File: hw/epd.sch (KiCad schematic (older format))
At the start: 26 parts, among them J1 Conn_01x24_MountingPin, Q2 Q_PMOS_GSD, Q3 IRLML6344, U2 LM75C

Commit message: epd-clock: hw v0.2
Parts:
- removed R4: 0, Resistor_SMD:R_0603_1608Metric, symbol Device:R
- added JP3: Jumper_3_Open, Jumper:SolderJumper-3_P1.3mm_Bridged12_RoundedPad1.0x1.5mm, symbol Jumper:Jumper_3_Open
- Q3: footprint Package_TO_SOT_SMD:SOT-23 -> Package_TO_SOT_SMD:SOT-323_SC-70
- renumbered R5 to R2, R6 to R3, R7 to R4
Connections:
- net BS1: now also JP3.2 (C)
- net GND: now also JP3.1 (A)
- net VCC: now also JP3.3 (B)
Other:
- note added: "3 wire spi"
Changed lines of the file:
@@
 $EndComp
 $Comp
-L power:GND #PWR024
+L power:GND #PWR025
 U 1 1 60F2B86E
 P 6900 2800
-F 0 "#PWR024" H 6900 2550 50  0001 C CNN
+F 0 "#PWR025" H 6900 2550 50  0001 C CNN
 F 1 "GND" H 6905 2627 50  0000 C CNN
 F 2 "" H 6900 2800 50  0001 C CNN
@@
 VGL
 $Comp
-L Device:R R5
+L Device:R R2
 U 1 1 60F42FB6
 P 5800 3300
-F 0 "R5" V 5700 3300 50  0000 C CNN
+F 0 "R2" V 5700 3300 50  0000 C CNN
 F 1 "4.7K" V 5900 3300 50  0000 C CNN
 F 2 "Resistor_SMD:R_0603_1608Metric" V 5730 3300 50  0001 C CNN
@@
 $EndComp
 $Comp
-L Device:R R6
+L Device:R R3
 U 1 1 60F4F067
 P 5800 3650
-F 0 "R6" V 5700 3650 50  0000 C CNN
+F 0 "R3" V 5700 3650 50  0000 C CNN
 F 1 "4.7K" V 5900 3650 50  0000 C CNN
 F 2 "Resistor_SMD:R_0603_1608Metric" V 5730 3650 50  0001 C CNN
@@
 F 0 "Q3" V 6342 5200 50  0000 C CNN
 F 1 "IRLML6344" V 6251 5200 50  0000 C CNN
-F 2 "Package_TO_SOT_SMD:SOT-23" H 6200 5300 50  0001 C CNN
+F 2 "Package_TO_SOT_SMD:SOT-323_SC-70" H 6200 5300 50  0001 C CNN
 F 3 "~" H 6000 5200 50  0001 C CNN
 	1    6000 5200
@@
 	6000 5400 6200 5400
 $Comp
-L Device:R R7
+L Device:R R4
 U 1 1 60FABFF4
 P 6300 4700
-F 0 "R7" H 6370 4746 50  0000 L CNN
+F 0 "R4" H 6370 4746 50  0000 L CNN
 F 1 "4.7" H 6370 4655 50  0000 L CNN
 F 2 "Resistor_SMD:R_0603_1608Metric" V 6230 4700 50  0001 C CNN
@@
 RESE
 $Comp
-L power:GND #PWR022
+L power:GND #PWR023
 U 1 1 60FAFD2B
 P 6300 4450
-F 0 "#PWR022" H 6300 4200 50  0001 C CNN
+F 0 "#PWR023" H 6300 4200 50  0001 C CNN
 F 1 "GND" H 6305 4277 50  0000 C CNN
 F 2 "" H 6300 4450 50  0001 C CNN
@@
 $EndComp
 $Comp
-L power:GND #PWR028
+L power:GND #PWR029
 U 1 1 60F34CE9
 P 8450 4200
-F 0 "#PWR028" H 8450 3950 50  0001 C CNN
+F 0 "#PWR029" H 8450 3950 50  0001 C CNN
 F 1 "GND" H 8455 4027 50  0000 C CNN
 F 2 "" H 8450 4200 50  0001 C CNN
@@
 $EndComp
 NoConn ~ 3300 2600
-Text Label 4200 3400 2    50   ~ 0
+Text Label 4500 3550 2    50   ~ 0
 BS1
-Text Notes 4300 3300 0    50   ~ 0
+Text Notes 4850 3350 0    50   ~ 0
 4 wire spi
 Text Label 4900 4400 0    50   ~ 0
@@
 $EndComp
 $Comp
-L power:GND #PWR013
+L power:GND #PWR014
 U 1 1 6105A8A0
 P 5000 2800
-F 0 "#PWR013" H 5000 2550 50  0001 C CNN
+F 0 "#PWR014" H 5000 2550 50  0001 C CNN
 F 1 "GND" H 5005 2627 50  0000 C CNN
 F 2 "" H 5000 2800 50  0001 C CNN
@@
 VPP
 $Comp
-L power:GND #PWR021
+L power:GND #PWR022
 U 1 1 6102F49A
 P 6200 2800
-F 0 "#PWR021" H 6200 2550 50  0001 C CNN
+F 0 "#PWR022" H 6200 2550 50  0001 C CNN
 F 1 "GND" H 6205 2627 50  0000 C CNN
 F 2 "" H 6200 2800 50  0001 C CNN
@@
 $EndComp
 $Comp
-L power:GND #PWR018
+L power:GND #PWR019
 U 1 1 60F2BEE7
 P 5825 2800
-F 0 "#PWR018" H 5825 2550 50  0001 C CNN
+F 0 "#PWR019" H 5825 2550 50  0001 C CNN
 F 1 "GND" H 5830 2627 50  0000 C CNN
 F 2 "" H 5825 2800 50  0001 C CNN
@@
 $EndComp
 $Comp
-L power:VCC #PWR029
+L power:VCC #PWR030
 U 1 1 610F51AE
 P 8650 3600
-F 0 "#PWR029" H 8650 3450 50  0001 C CNN
+F 0 "#PWR030" H 8650 3450 50  0001 C CNN
 F 1 "VCC" H 8550 3750 50  0000 L CNN
 F 2 "" H 8650 3600 50  0001 C CNN
@@
 $EndComp
 $Comp
-L power:VCC #PWR016
+L power:VCC #PWR017
 U 1 1 61124FF6
 P 5400 5850
-F 0 "#PWR016" H 5400 5700 50  0001 C CNN
+F 0 "#PWR017" H 5400 5700 50  0001 C CNN
 F 1 "VCC" V 5400 5975 50  0000 L CNN
 F 2 "" H 5400 5850 50  0001 C CNN
@@
 $EndComp
 $Comp
-L power:GND #PWR023
+L power:GND #PWR024
 U 1 1 611B06C7
 P 6550 2800
-F 0 "#PWR023" H 6550 2550 50  0001 C CNN
+F 0 "#PWR024" H 6550 2550 50  0001 C CNN
 F 1 "GND" H 6555 2627 50  0000 C CNN
 F 2 "" H 6550 2800 50  0001 C CNN
@@
 $EndComp
 $Comp
-L power:GND #PWR025
+L power:GND #PWR026
 U 1 1 611B425C
 P 7250 2800
-F 0 "#PWR025" H 7250 2550 50  0001 C CNN
+F 0 "#PWR026" H 7250 2550 50  0001 C CNN
 F 1 "GND" H 7255 2627 50  0000 C CNN
 F 2 "" H 7250 2800 50  0001 C CNN
@@
 $EndComp
 $Comp
-L power:VCC #PWR026
+L power:VCC #PWR027
 U 1 1 611B867C
 P 7950 3200
-F 0 "#PWR026" H 7950 3050 50  0001 C CNN
+F 0 "#PWR027" H 7950 3050 50  0001 C CNN
 F 1 "VCC" H 7965 3373 50  0000 C CNN
 F 2 "" H 7950 3200 50  0001 C CNN
@@
 $EndComp
 $Comp
-L power:VCC #PWR019
+L power:VCC #PWR020
 U 1 1 611BC164
 P 5950 3300
-F 0 "#PWR019" H 5950 3150 50  0001 C CNN
+F 0 "#PWR020" H 5950 3150 50  0001 C CNN
 F 1 "VCC" V 5965 3428 50  0000 L CNN
 F 2 "" H 5950 3300 50  0001 C CNN
@@
 $EndComp
 $Comp
-L power:VCC #PWR020
+L power:VCC #PWR021
 U 1 1 611C3951
 P 5950 3650
-F 0 "#PWR020" H 5950 3500 50  0001 C CNN
+F 0 "#PWR021" H 5950 3500 50  0001 C CNN
 F 1 "VCC" V 5965 3778 50  0000 L CNN
 F 2 "" H 5950 3650 50  0001 C CNN
@@
 $EndComp
 $Comp
-L Device:R R4
-U 1 1 60FEDBD7
-P 4500 3400
-F 0 "R4" V 4550 3550 50  0000 C CNN
-F 1 "0" V 4500 3400 50  0000 C CNN
-F 2 "Resistor_SMD:R_0603_1608Metric" V 4430 3400 50  0001 C CNN
-F 3 "~" H 4500 3400 50  0001 C CNN
-	1    4500 3400
-	0    1    1    0
-$EndComp
-$Comp
 L power:GND #PWR012
 U 1 1 611E4B10
-P 4700 3400
-F 0 "#PWR012" H 4700 3150 50  0001 C CNN
-F 1 "GND" V 4705 3272 50  0000 R CNN
-F 2 "" H 4700 3400 50  0001 C CNN
-F 3 "" H 4700 3400 50  0001 C CNN
-	1    4700 3400
-	0    -1   -1   0
+P 4650 3300
+F 0 "#PWR012" H 4650 3050 50  0001 C CNN
+F 1 "GND" H 4550 3200 50  0000 R CNN
+F 2 "" H 4650 3300 50  0001 C CNN
+F 3 "" H 4650 3300 50  0001 C CNN
+	1    4650 3300
+	-1   0    0    1
 $EndComp
 Wire Wire Line
@@
 	8350 3800 8350 4200
 $Comp
-L power:GND #PWR015
+L power:GND #PWR016
 U 1 1 611EE51A
 P 5000 5650
-F 0 "#PWR015" H 5000 5400 50  0001 C CNN
+F 0 "#PWR016" H 5000 5400 50  0001 C CNN
 F 1 "GND" V 5005 5522 50  0000 R CNN
 F 2 "" H 5000 5650 50  0001 C CNN
@@
 $EndComp
 $Comp
-L power:GND #PWR017
+L power:GND #PWR018
 U 1 1 611FBD36
 P 5450 2800
-F 0 "#PWR017" H 5450 2550 50  0001 C CNN
+F 0 "#PWR018" H 5450 2550 50  0001 C CNN
 F 1 "GND" H 5455 2627 50  0000 C CNN
 F 2 "" H 5450 2800 50  0001 C CNN
@@
 	5400 4100 5400 4600
 $Comp
-L power:GND #PWR014
+L power:GND #PWR015
 U 1 1 6121586C
 P 5000 4100
-F 0 "#PWR014" H 5000 3850 50  0001 C CNN
+F 0 "#PWR015" H 5000 3850 50  0001 C CNN
 F 1 "GND" V 5005 3972 50  0000 R CNN
 F 2 "" H 5000 4100 50  0001 C CNN
@@
 $EndComp
 $Comp
-L power:GND #PWR027
+L power:GND #PWR028
 U 1 1 61226EC7
 P 7950 4200
-F 0 "#PWR027" H 7950 3950 50  0001 C CNN
+F 0 "#PWR028" H 7950 3950 50  0001 C CNN
 F 1 "GND" H 7955 4027 50  0000 C CNN
 F 2 "" H 7950 4200 50  0001 C CNN
@@
 $EndComp
 $Comp
-L power:GND #PWR030
+L power:GND #PWR031
 U 1 1 6122A035
 P 8650 3900
-F 0 "#PWR030" H 8650 3650 50  0001 C CNN
+F 0 "#PWR031" H 8650 3650 50  0001 C CNN
 F 1 "GND" H 8655 3727 50  0000 C CNN
 F 2 "" H 8650 3900 50  0001 C CNN
@@
 	1    0    0    -1
 $EndComp
-Wire Wire Line
-	4650 3400 4700 3400
-$Comp
-L power:PWR_FLAG #FLG03
+$Comp
+L power:PWR_FLAG #FLG04
 U 1 1 6101A186
 P 1900 4900
-F 0 "#FLG03" H 1900 4975 50  0001 C CNN
+F 0 "#FLG04" H 1900 4975 50  0001 C CNN
 F 1 "PWR_FLAG" H 1900 5073 50  0000 C CNN
 F 2 "" H 1900 4900 50  0001 C CNN
@@
 	1650 4900 1900 4900
 Connection ~ 1650 4900
-Wire Wire Line
-	4200 3400 4350 3400
+$Comp
+L Jumper:Jumper_3_Open JP3
+U 1 1 61189634
+P 4650 3550
+F 0 "JP3" V 4604 3637 50  0000 L CNN
+F 1 "Jumper_3_Open" V 4695 3637 50  0000 L CNN
+F 2 "Jumper:SolderJumper-3_P1.3mm_Bridged12_RoundedPad1.0x1.5mm" H 4650 3550 50  0001 C CNN
+F 3 "~" H 4650 3550 50  0001 C CNN
+	1    4650 3550
+	0    1    1    0
+$EndComp
+$Comp
+L power:VCC #PWR013
+U 1 1 6119CF05
+P 4650 3800
+F 0 "#PWR013" H 4650 3650 50  0001 C CNN
+F 1 "VCC" H 4450 3900 50  0000 L CNN
+F 2 "" H 4650 3800 50  0001 C CNN
+F 3 "" H 4650 3800 50  0001 C CNN
+	1    4650 3800
+	-1   0    0    1
+$EndComp
+Text Notes 4850 3750 0    50   ~ 0
+3 wire spi
 $EndSCHEMATC

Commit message: epd-clock: hw change C8 footprint
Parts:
- C8: footprint Capacitor_SMD:C_0603_1608Metric -> Capacitor_SMD:C_1206_3216Metric
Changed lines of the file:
@@
 F 0 "C8" V 5000 5100 50  0000 C CNN
 F 1 "4.7uF/50V" V 5300 5100 50  0000 C CNN
-F 2 "Capacitor_SMD:C_0603_1608Metric" H 5188 4950 50  0001 C CNN
+F 2 "Capacitor_SMD:C_1206_3216Metric" H 5188 4950 50  0001 C CNN
 F 3 "~" H 5150 5100 50  0001 C CNN
 	1    5150 5100

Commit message: epd-clock: hw: v0.2
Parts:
- removed C16: 0.1uF, Capacitor_SMD:C_0603_1608Metric, symbol Device:C
- removed JP3: Jumper_3_Open, Jumper:SolderJumper-3_P1.3mm_Bridged12_RoundedPad1.0x1.5mm, symbol Jumper:Jumper_3_Open
- removed U2: LM75C, Package_SO:SO-8_5.3x6.2mm_P1.27mm, symbol Sensor_Temperature:LM75C
- added R2, R3: 10K, Resistor_SMD:R_0603_1608Metric, symbol Device:R
- C10: renamed from C8; value 4.7uF/50V -> 0.1uF/50V; footprint Capacitor_SMD:C_1206_3216Metric -> Capacitor_SMD:C_0603_1608Metric
- renumbered C12 to C11, C5 to C12, C6 to C3, C3 to C4, C4 to C5, C9 to C6, C10 to C7, C11 to C8, C7 to C9, R2 to R5, R3 to R6
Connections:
- net BS1 is gone; now on net GND: J1.8 (Pin_8)
- net BUSY: now also J1.16 (Pin_16); no longer J1.9 (Pin_9)
- net CLK: now also J1.12 (Pin_12); no longer J1.13 (Pin_13)
- net CS#: now also J1.13 (Pin_13); no longer J1.12 (Pin_12)
- net DC#: now also J1.14 (Pin_14); no longer J1.11 (Pin_11)
- net DIN: now also J1.11 (Pin_11); no longer J1.14 (Pin_14)
- net GDR: now also J1.23 (Pin_23), R3.1; no longer J1.2 (Pin_2)
- net GND: now also C6.1, R4.2, R3.2; no longer C6.2, R4.1
- net NC: now also J1.24 (Pin_24); no longer J1.1 (Pin_1)
- net PREVGH: now also J1.4 (Pin_4); no longer J1.21 (Pin_21)
- net PREVGL: now also J1.2 (Pin_2); no longer J1.23 (Pin_23)
- net PWR: now also R2.1
- net PWR_EN#: now also R2.2
- net RESE: now also J1.22 (Pin_22), R4.1; no longer J1.3 (Pin_3), R4.2
- net RST#: now also J1.15 (Pin_15); no longer J1.10 (Pin_10)
- net TSCL: now also J1.19 (Pin_19); no longer J1.6 (Pin_6)
- net TSDA: now also J1.18 (Pin_18); no longer J1.7 (Pin_7)
- net VCC: now also C6.2, J1.10 (Pin_10), J1.9 (Pin_9); no longer C6.1, J1.15 (Pin_15), J1.16 (Pin_16)
- net VCOM: now also J1.1 (Pin_1); no longer J1.24 (Pin_24)
- net VDD: now also J1.7 (Pin_7); no longer J1.18 (Pin_18)
- net VGH: now also J1.20 (Pin_20); no longer J1.5 (Pin_5)
- net VGL: now also J1.21 (Pin_21); no longer J1.4 (Pin_4)
- net VPP: now also J1.6 (Pin_6); no longer J1.19 (Pin_19)
- net VSH: now also J1.5 (Pin_5); no longer J1.20 (Pin_20)
- net VSL: now also J1.3 (Pin_3); no longer J1.22 (Pin_22)
- no-connect marks 2 -> 1
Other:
- note added: "2R2\n3R\n0.47R"
- note removed: "3 wire spi"
- moved on the sheet: C10, C11, C12, C13, C14, C15, C3, C4, C5, C6, C7, C8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

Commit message: epd-clock: hw v0.2
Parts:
- C10: footprint Capacitor_SMD:C_0603_1608Metric -> Capacitor_SMD:C_0805_2012Metric
- Q3: footprint Package_TO_SOT_SMD:SOT-323_SC-70 -> Package_TO_SOT_SMD:SOT-23
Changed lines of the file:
@@
 F 0 "C10" H 7000 4350 50  0000 C CNN
 F 1 "0.1uF/50V" H 7150 4450 50  0000 C CNN
-F 2 "Capacitor_SMD:C_0603_1608Metric" H 6888 4250 50  0001 C CNN
+F 2 "Capacitor_SMD:C_0805_2012Metric" H 6888 4250 50  0001 C CNN
 F 3 "~" H 6850 4400 50  0001 C CNN
 	1    6850 4400
@@
 F 0 "Q3" H 7000 5050 50  0000 C CNN
 F 1 "IRLML6344" H 7150 4950 50  0000 C CNN
-F 2 "Package_TO_SOT_SMD:SOT-323_SC-70" H 6950 5100 50  0001 C CNN
+F 2 "Package_TO_SOT_SMD:SOT-23" H 6950 5100 50  0001 C CNN
 F 3 "~" H 6750 5000 50  0001 C CNN
 	1    6750 5000

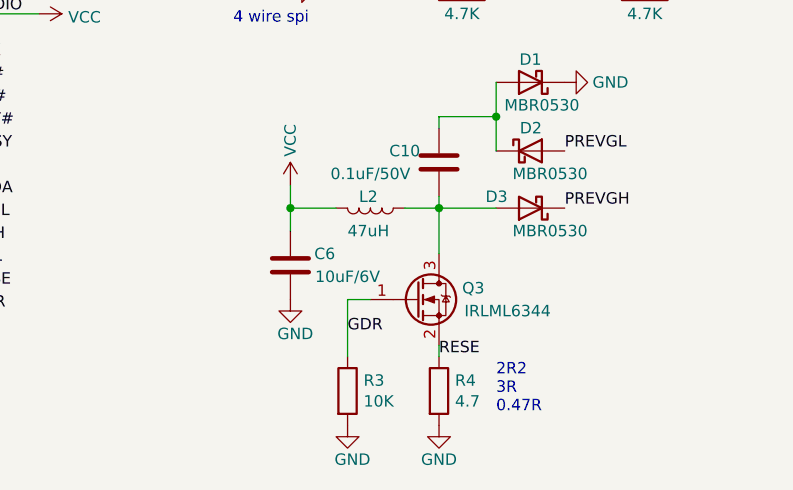
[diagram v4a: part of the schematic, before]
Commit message: hw: 修正几个元件的参数
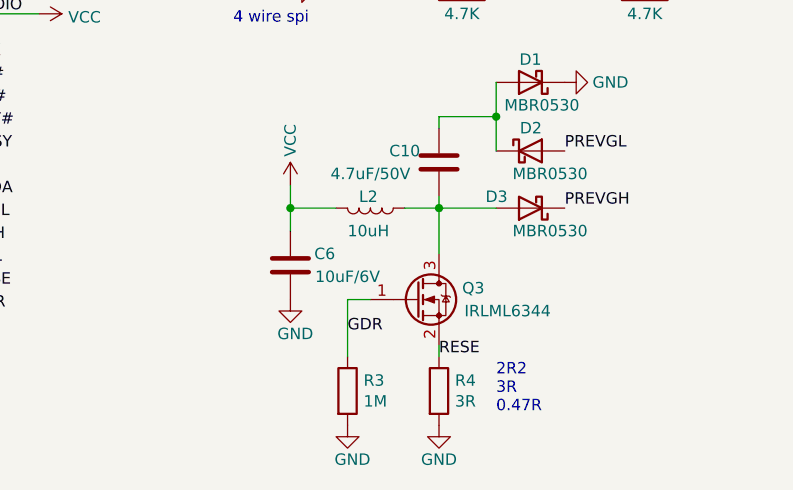
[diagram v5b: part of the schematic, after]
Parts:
- C10: value 0.1uF/50V -> 4.7uF/50V
- L2: value 47uH -> 10uH
- R3: value 10K -> 1M
- R4: value 4.7 -> 3R
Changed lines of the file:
@@
 P 6850 4400
 F 0 "C10" H 7000 4350 50  0000 C CNN
-F 1 "0.1uF/50V" H 7150 4450 50  0000 C CNN
+F 1 "4.7uF/50V" H 7150 4450 50  0000 C CNN
 F 2 "Capacitor_SMD:C_0805_2012Metric" H 6888 4250 50  0001 C CNN
 F 3 "~" H 6850 4400 50  0001 C CNN
@@
 P 6550 4600
 F 0 "L2" V 6500 4550 50  0000 L CNN
-F 1 "47uH" V 6650 4500 50  0000 L CNN
+F 1 "10uH" V 6650 4500 50  0000 L CNN
 F 2 "Inductor_SMD:L_Coilcraft_XxL4020" H 6550 4600 50  0001 C CNN
 F 3 "~" H 6550 4600 50  0001 C CNN
@@
 P 6450 5400
 F 0 "R3" H 6520 5446 50  0000 L CNN
-F 1 "10K" H 6520 5355 50  0000 L CNN
+F 1 "1M" H 6520 5355 50  0000 L CNN
 F 2 "Resistor_SMD:R_0603_1608Metric" V 6380 5400 50  0001 C CNN
 F 3 "~" H 6450 5400 50  0001 C CNN
@@
 P 6850 5400
 F 0 "R4" H 6920 5446 50  0000 L CNN
-F 1 "4.7" H 6920 5355 50  0000 L CNN
+F 1 "3R" H 6920 5355 50  0000 L CNN
 F 2 "Resistor_SMD:R_0603_1608Metric" V 6780 5400 50  0001 C CNN
 F 3 "~" H 6850 5400 50  0001 C CNN

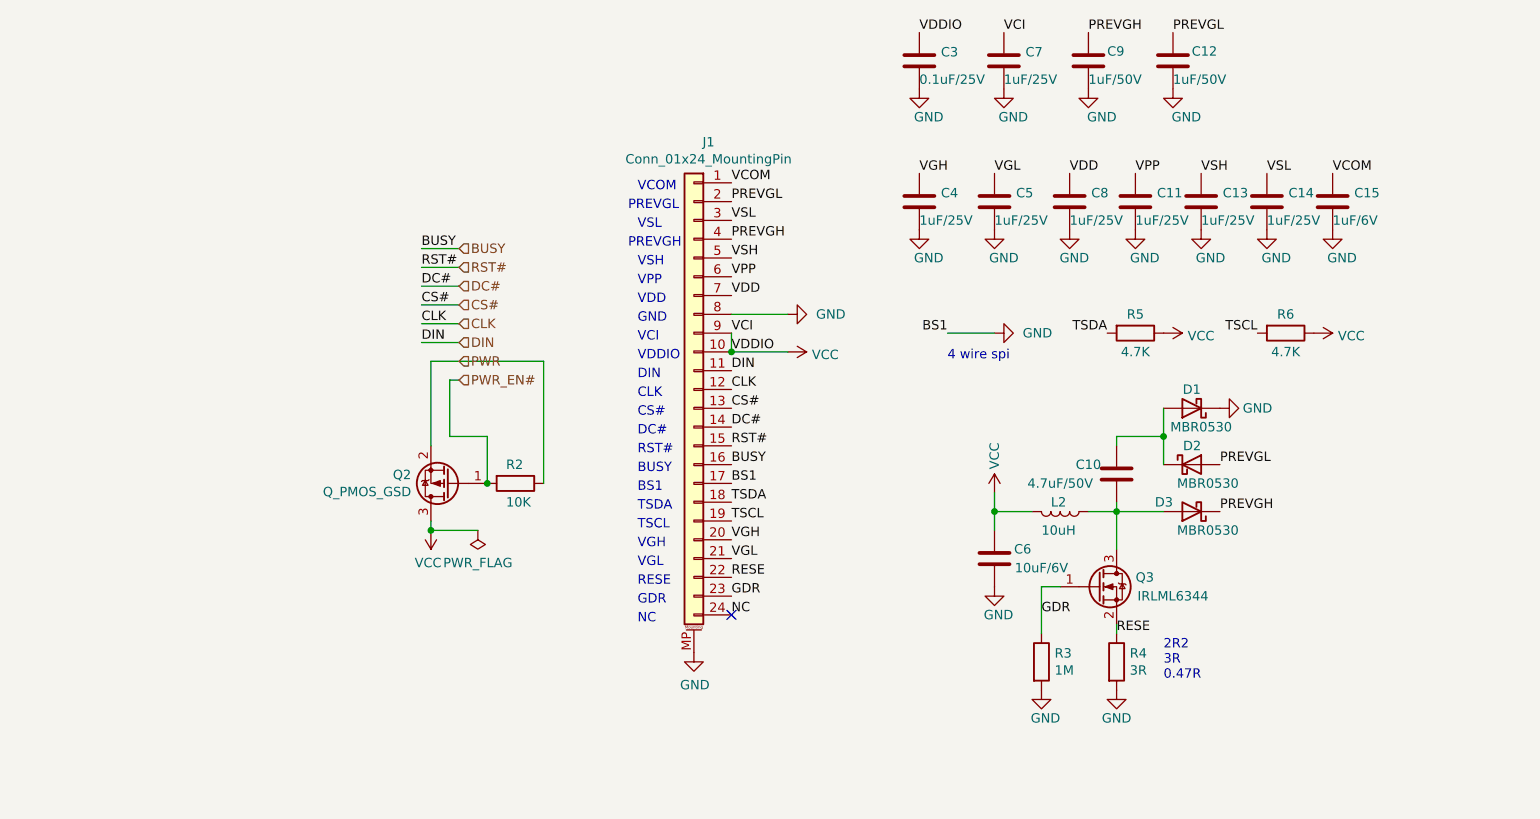
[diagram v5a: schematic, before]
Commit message: hw: 合并电源网络
取消墨水屏电源控制mos与独立电源域，墨水屏使用深度休眠模式，共用主
电源域。
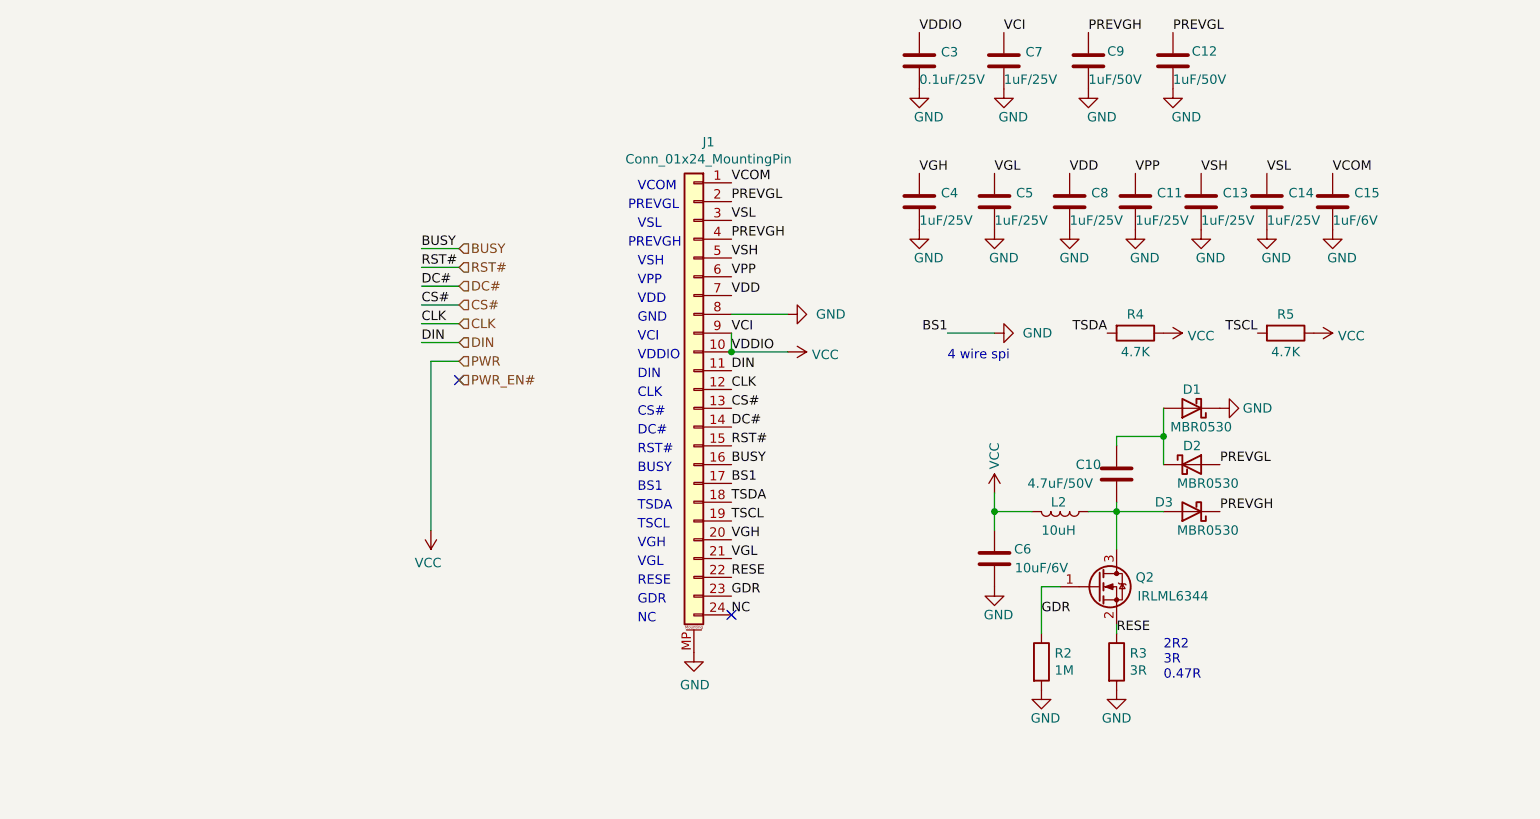
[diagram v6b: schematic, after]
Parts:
- removed Q2: Q_PMOS_GSD, Package_TO_SOT_SMD:SOT-23, symbol Device:Q_PMOS_GSD
- removed R2: 10K, Resistor_SMD:R_0603_1608Metric, symbol Device:R
- renumbered Q3 to Q2, R3 to R2, R4 to R3, R5 to R4, R6 to R5
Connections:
- no-connect marks 1 -> 2
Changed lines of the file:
@@
 VGL
 $Comp
-L Device:R R5
+L Device:R R4
 U 1 1 60F42FB6
 P 6950 3650
-F 0 "R5" V 6850 3650 50  0000 C CNN
+F 0 "R4" V 6850 3650 50  0000 C CNN
 F 1 "4.7K" V 7050 3650 50  0000 C CNN
 F 2 "Resistor_SMD:R_0603_1608Metric" V 6880 3650 50  0001 C CNN
@@
 $EndComp
 $Comp
-L Device:R R6
+L Device:R R5
 U 1 1 60F4F067
 P 7750 3650
-F 0 "R6" V 7650 3650 50  0000 C CNN
+F 0 "R5" V 7650 3650 50  0000 C CNN
 F 1 "4.7K" V 7850 3650 50  0000 C CNN
 F 2 "Resistor_SMD:R_0603_1608Metric" V 7680 3650 50  0001 C CNN
@@
 $EndComp
 $Comp
-L Device:Q_NMOS_GSD Q3
+L Device:Q_NMOS_GSD Q2
 U 1 1 60FA58A2
 P 6750 5000
-F 0 "Q3" H 7000 5050 50  0000 C CNN
+F 0 "Q2" H 7000 5050 50  0000 C CNN
 F 1 "IRLML6344" H 7150 4950 50  0000 C CNN
 F 2 "Package_TO_SOT_SMD:SOT-23" H 6950 5100 50  0001 C CNN
@@
 Text HLabel 3350 3800 2    50   Input ~ 0
 PWR
-Text HLabel 3350 3900 2    50   Input ~ 0
-PWR_EN#
-$Comp
-L Device:Q_PMOS_GSD Q2
-U 1 1 61196E7E
-P 3300 4450
-F 0 "Q2" H 3505 4404 50  0000 L CNN
-F 1 "Q_PMOS_GSD" H 3505 4495 50  0000 L CNN
-F 2 "Package_TO_SOT_SMD:SOT-23" H 3500 4550 50  0001 C CNN
-F 3 "~" H 3300 4450 50  0001 C CNN
-	1    3300 4450
-	-1   0    0    1
-$EndComp
-Wire Wire Line
-	3200 3800 3200 4250
-Wire Wire Line
-	3300 3900 3300 4200
-Wire Wire Line
-	3300 4200 3500 4200
-Wire Wire Line
-	3500 4200 3500 4450
-Wire Wire Line
-	3300 3900 3350 3900
 $Comp
 L power:VCC #PWR04
@@
 	1    0    0    -1
 $EndComp
-$Comp
-L power:PWR_FLAG #FLG04
-U 1 1 6101A186
-P 3450 4700
-F 0 "#FLG04" H 3450 4775 50  0001 C CNN
-F 1 "PWR_FLAG" H 3450 4873 50  0000 C CNN
-F 2 "" H 3450 4700 50  0001 C CNN
-F 3 "~" H 3450 4700 50  0001 C CNN
-	1    3450 4700
-	-1   0    0    1
-$EndComp
-Wire Wire Line
-	3200 4650 3200 4700
-Wire Wire Line
-	3200 4700 3450 4700
-Connection ~ 3200 4700
 Text Notes 4300 5200 0    50   ~ 0
 NC
@@
 	6850 4600 7100 4600
 $Comp
-L Device:R R3
+L Device:R R2
 U 1 1 613BA793
 P 6450 5400
-F 0 "R3" H 6520 5446 50  0000 L CNN
+F 0 "R2" H 6520 5446 50  0000 L CNN
 F 1 "1M" H 6520 5355 50  0000 L CNN
 F 2 "Resistor_SMD:R_0603_1608Metric" V 6380 5400 50  0001 C CNN
@@
 $EndComp
 $Comp
-L Device:R R4
+L Device:R R3
 U 1 1 613C295F
 P 6850 5400
-F 0 "R4" H 6920 5446 50  0000 L CNN
+F 0 "R3" H 6920 5446 50  0000 L CNN
 F 1 "3R" H 6920 5355 50  0000 L CNN
 F 2 "Resistor_SMD:R_0603_1608Metric" V 6780 5400 50  0001 C CNN
@@
 Wire Wire Line
 	6850 5250 6850 5200
-$Comp
-L Device:R R2
-U 1 1 611B9AD3
-P 3650 4450
-F 0 "R2" V 3550 4400 50  0000 L CNN
-F 1 "10K" V 3750 4400 50  0000 L CNN
-F 2 "Resistor_SMD:R_0603_1608Metric" V 3580 4450 50  0001 C CNN
-F 3 "~" H 3650 4450 50  0001 C CNN
-	1    3650 4450
-	0    1    1    0
-$EndComp
-Connection ~ 3500 4450
-Wire Wire Line
-	3800 3800 3800 4450
-Wire Wire Line
-	3200 3800 3800 3800
+Text HLabel 3350 3900 2    50   Input ~ 0
+PWR_EN#
+Wire Wire Line
+	3200 3800 3350 3800
+Wire Wire Line
+	3200 3800 3200 4700
+NoConn ~ 3350 3900
 $EndSCHEMATC
